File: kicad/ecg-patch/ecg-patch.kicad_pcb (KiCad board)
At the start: 2 copper layers, 94 x 26 mm, 9 parts

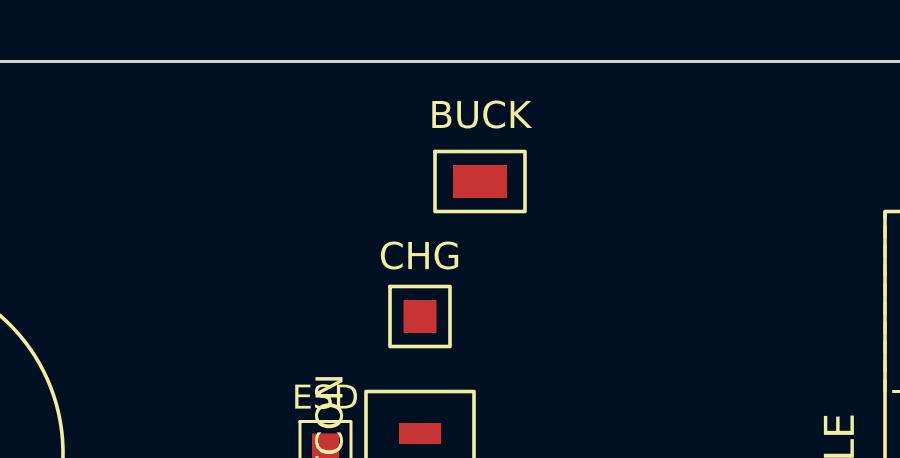
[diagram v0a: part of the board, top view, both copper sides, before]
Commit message: Replace editor UI with Astra tinybot
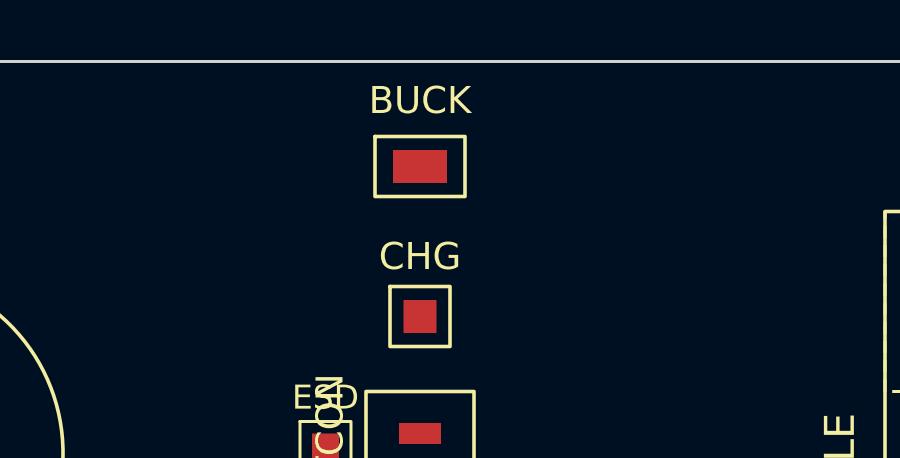
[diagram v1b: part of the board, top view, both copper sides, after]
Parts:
- moved BUCK 2.06 mm to (47.0, 3.50)
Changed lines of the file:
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@@
   )
   (footprint "MissionPCB:BUCK_Demo" (layer "F.Cu")
-    (at 49 4 0)
+    (at 47 3.5 0)
     (property "Reference" "BUCK" (at 0 -2.2 0) (layer "F.SilkS") (effects (font (size 0.9 0.9) (thickness 0.12))))
     (property "Value" "TPS62740" (at 0 2.2 0) (layer "F.Fab") (effects (font (size 0.7 0.7) (thickness 0.1))))
